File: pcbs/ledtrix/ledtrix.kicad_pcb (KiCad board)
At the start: 2 copper layers, 40.6 x 46.7 mm, 153 parts, among them J1 Conn, J2 Conn

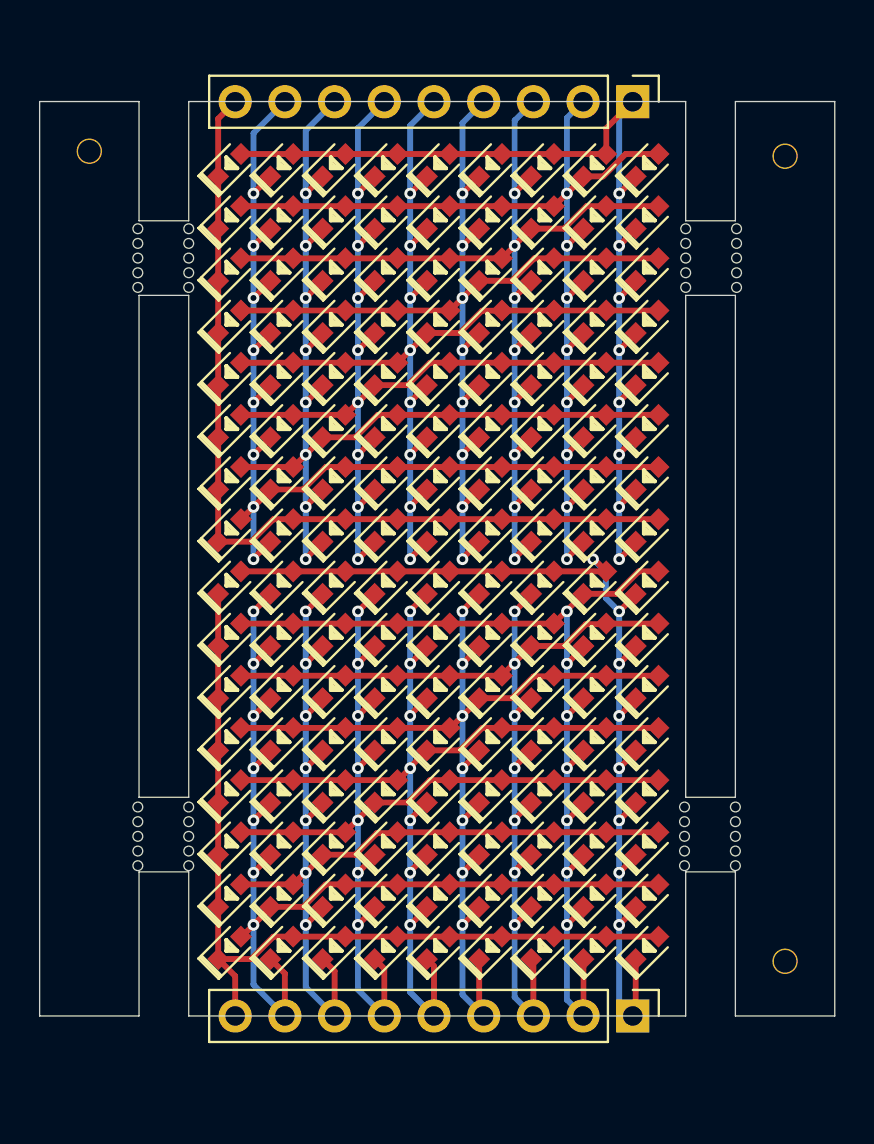
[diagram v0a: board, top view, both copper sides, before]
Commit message: Make some boards with just the LEDs
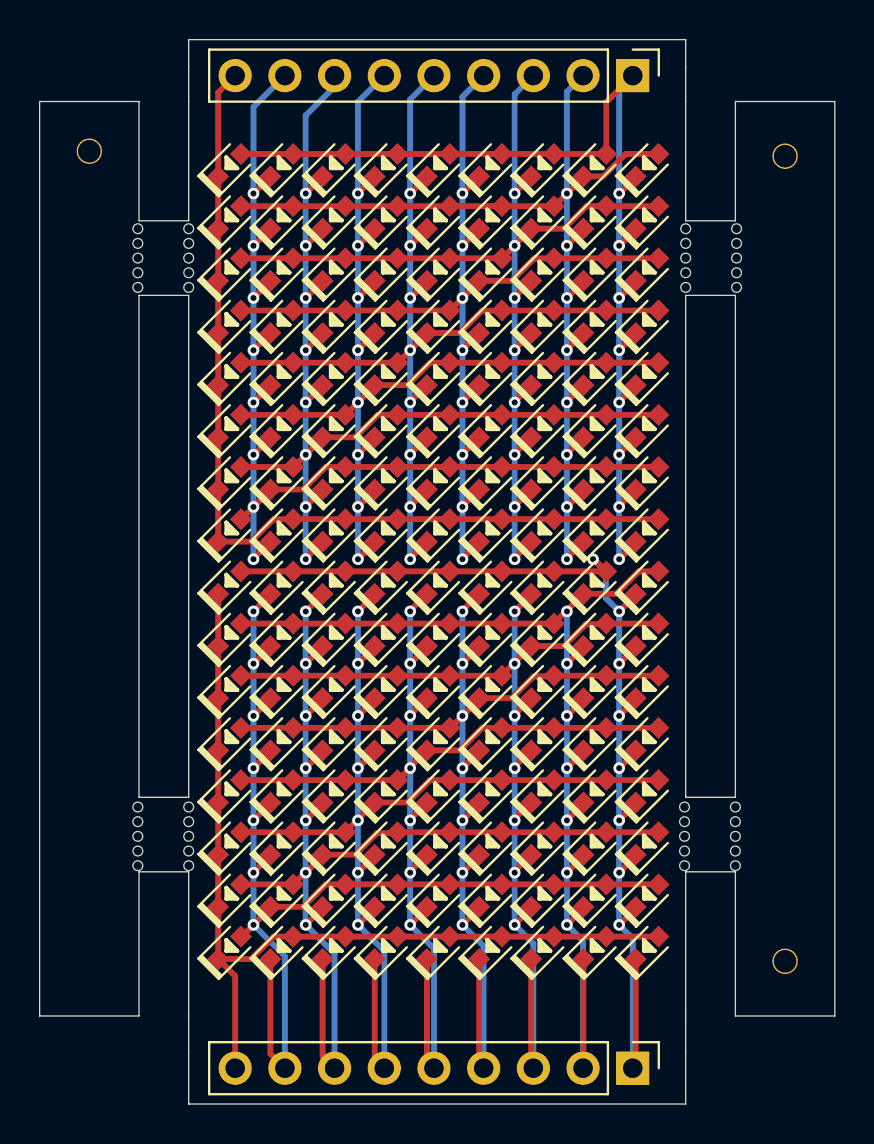
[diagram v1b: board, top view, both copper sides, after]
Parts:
- moved J2 2.67 mm to (199.9, 109.2)
- moved J1 1.34 mm to (199.9, 58.4)
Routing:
- net /CB6: track 54.3 -> 59.7 mm
- net /CB3: track 54.1 -> 59.4 mm
- net /CB2: track 54.0 -> 59.3 mm
- net /CB1: track 55.6 -> 60.9 mm
- net /CB8: track 54.6 -> 60.0 mm
- net /CB7: track 54.5 -> 59.8 mm
- net /CB5: track 54.3 -> 59.6 mm
- net /CB4: track 54.2 -> 59.5 mm
- net /CB9: track 44.9 -> 47.6 mm
- net /CA1: track 55.5 -> 58.1 mm
- net /CA7: track 55.1 -> 56.5 mm
- net /CA6: track 55.1 -> 56.4 mm
- net /CA9: track 45.8 -> 47.2 mm
- net /CA8: track 55.2 -> 56.5 mm
- net /CA5: track 55.0 -> 56.4 mm
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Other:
- board size 40.6 x 46.7 mm -> 40.6 x 54.4 mm
